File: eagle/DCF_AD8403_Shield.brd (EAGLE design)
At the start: 81 x 53.3 mm, 24 parts, among them IC1 TL072P, IC2 AD8403-100, J1 DCIN

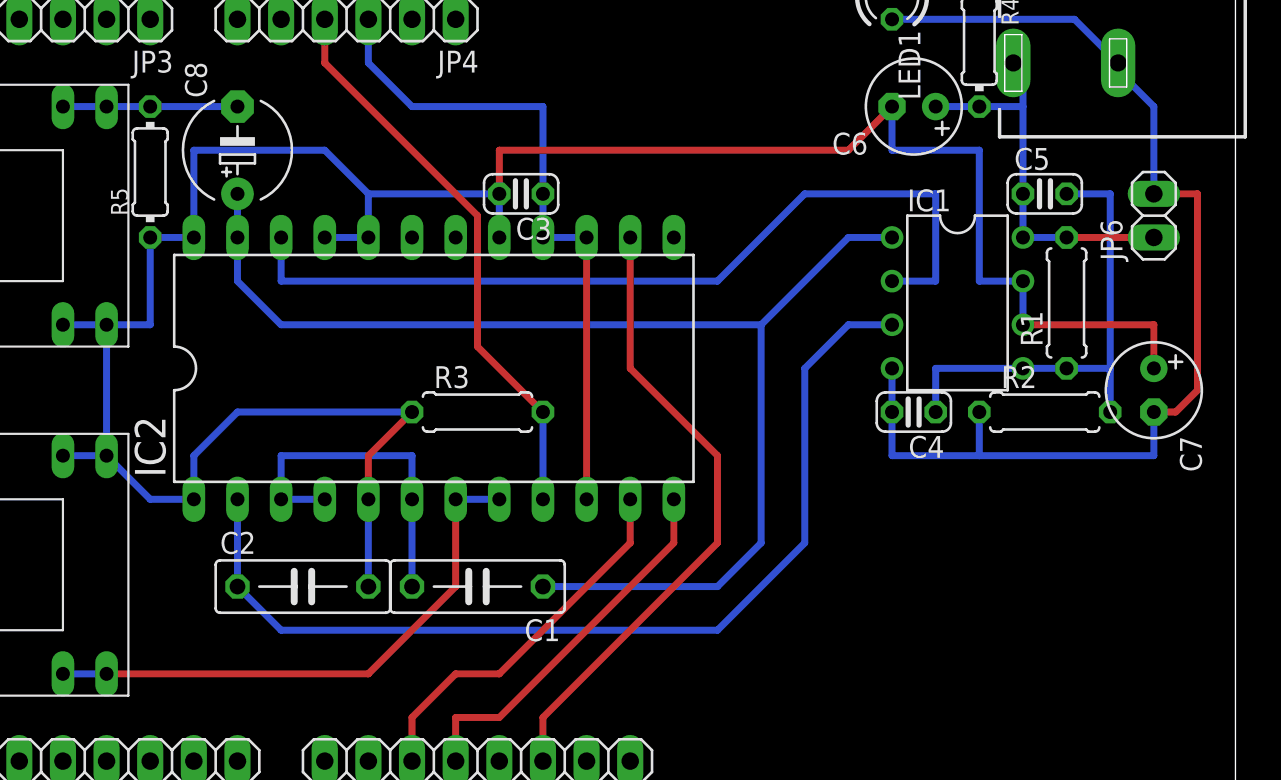
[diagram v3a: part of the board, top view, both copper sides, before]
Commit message: Remove: Decoupling Capacitor of OPAMP
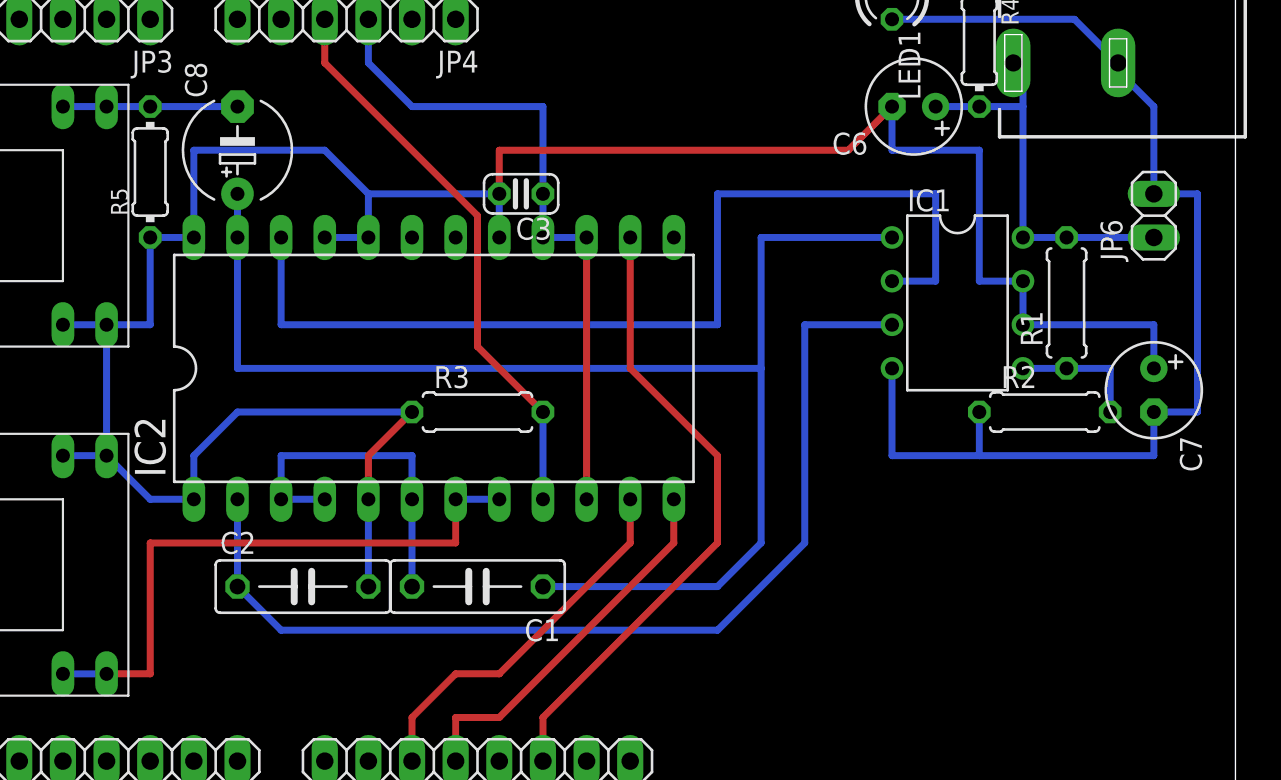
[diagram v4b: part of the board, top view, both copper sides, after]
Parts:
- removed C4, C5: 0.1uF, rcl:C025-024X044
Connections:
- net N$5: no longer C4.1, C5.2
- net V+: no longer C5.1
- net V-: no longer C4.2
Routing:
- net N$5: track 27.9 -> 7.62 mm
- net N$1: track 50.4 -> 58.4 mm
- net FILTERED: track 72.8 -> 79.8 mm
- net BYPASS: track 32.6 -> 35.6 mm
- net N$8: track 57.5 -> 59.0 mm
- net V-: track 65.1 -> 65.9 mm
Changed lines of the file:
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@@
 <element name="R1" library="rcl" package="0207/7" value="100k" x="71.12" y="31.75" rot="R90"/>
 <element name="R2" library="rcl" package="0207/7" value="100k" x="69.85" y="25.4"/>
-<element name="C4" library="rcl" package="C025-024X044" value="0.1uF" x="62.23" y="25.4" rot="R180"/>
-<element name="C5" library="rcl" package="C025-024X044" value="0.1uF" x="69.85" y="38.1"/>
 <element name="C6" library="rcl" package="E2,5-6" value="100uF" x="62.23" y="43.18" rot="R180"/>
 <element name="C7" library="rcl" package="E2,5-6" value="100uF" x="76.2" y="26.67" rot="R270"/>
@@
 <wire x1="12.7" y1="10.16" x2="15.24" y2="10.16" width="0.4064" layer="16"/>
 <wire x1="35.56" y1="20.32" x2="38.1" y2="20.32" width="0.4064" layer="16"/>
-<wire x1="15.24" y1="10.16" x2="30.48" y2="10.16" width="0.4064" layer="1"/>
-<wire x1="30.48" y1="10.16" x2="35.56" y2="15.24" width="0.4064" layer="1"/>
-<wire x1="35.56" y1="15.24" x2="35.56" y2="20.32" width="0.4064" layer="1"/>
+<wire x1="17.78" y1="17.78" x2="35.56" y2="17.78" width="0.4064" layer="1"/>
+<wire x1="35.56" y1="17.78" x2="35.56" y2="20.32" width="0.4064" layer="1"/>
+<wire x1="15.24" y1="10.16" x2="17.78" y2="10.16" width="0.4064" layer="1"/>
+<wire x1="17.78" y1="10.16" x2="17.78" y2="17.78" width="0.4064" layer="1"/>
 </signal>
 <signal name="+5V">
@@
 <wire x1="25.4" y1="12.7" x2="50.8" y2="12.7" width="0.4064" layer="16"/>
 <wire x1="50.8" y1="12.7" x2="55.88" y2="17.78" width="0.4064" layer="16"/>
-<wire x1="55.88" y1="17.78" x2="55.88" y2="27.94" width="0.4064" layer="16"/>
-<wire x1="58.42" y1="30.48" x2="60.96" y2="30.48" width="0.4064" layer="16"/>
-<wire x1="55.88" y1="27.94" x2="58.42" y2="30.48" width="0.4064" layer="16"/>
+<wire x1="55.88" y1="17.78" x2="55.88" y2="30.48" width="0.4064" layer="16"/>
+<wire x1="55.88" y1="30.48" x2="60.96" y2="30.48" width="0.4064" layer="16"/>
 </signal>
 <signal name="FILTERED">
@@
 <contactref element="IC1" pad="1"/>
 <contactref element="IC2" pad="23"/>
-<wire x1="22.86" y1="35.56" x2="22.86" y2="33.02" width="0.4064" layer="16"/>
-<wire x1="22.86" y1="33.02" x2="25.4" y2="30.48" width="0.4064" layer="16"/>
-<wire x1="25.4" y1="30.48" x2="53.34" y2="30.48" width="0.4064" layer="16"/>
+<wire x1="22.86" y1="35.56" x2="22.86" y2="27.94" width="0.4064" layer="16"/>
+<wire x1="22.86" y1="27.94" x2="53.34" y2="27.94" width="0.4064" layer="16"/>
 <wire x1="40.64" y1="15.24" x2="50.8" y2="15.24" width="0.4064" layer="16"/>
 <wire x1="50.8" y1="15.24" x2="53.34" y2="17.78" width="0.4064" layer="16"/>
-<wire x1="53.34" y1="17.78" x2="53.34" y2="30.48" width="0.4064" layer="16"/>
-<wire x1="53.34" y1="30.48" x2="58.42" y2="35.56" width="0.4064" layer="16"/>
-<wire x1="58.42" y1="35.56" x2="60.96" y2="35.56" width="0.4064" layer="16"/>
+<wire x1="53.34" y1="17.78" x2="53.34" y2="27.94" width="0.4064" layer="16"/>
+<wire x1="53.34" y1="27.94" x2="53.34" y2="35.56" width="0.4064" layer="16"/>
+<wire x1="53.34" y1="35.56" x2="60.96" y2="35.56" width="0.4064" layer="16"/>
 <contactref element="C8" pad="+"/>
 <wire x1="22.86" y1="38.1" x2="22.86" y2="35.56" width="0.4064" layer="16"/>
@@
 <contactref element="IC1" pad="2"/>
 <contactref element="IC2" pad="22"/>
-<wire x1="25.4" y1="35.56" x2="25.4" y2="33.02" width="0.4064" layer="16"/>
+<wire x1="25.4" y1="35.56" x2="25.4" y2="30.48" width="0.4064" layer="16"/>
 <wire x1="63.5" y1="33.02" x2="60.96" y2="33.02" width="0.4064" layer="16"/>
-<wire x1="25.4" y1="33.02" x2="50.8" y2="33.02" width="0.4064" layer="16"/>
-<wire x1="55.88" y1="38.1" x2="63.5" y2="38.1" width="0.4064" layer="16"/>
+<wire x1="25.4" y1="30.48" x2="50.8" y2="30.48" width="0.4064" layer="16"/>
+<wire x1="50.8" y1="38.1" x2="63.5" y2="38.1" width="0.4064" layer="16"/>
 <wire x1="63.5" y1="38.1" x2="63.5" y2="33.02" width="0.4064" layer="16"/>
-<wire x1="50.8" y1="33.02" x2="55.88" y2="38.1" width="0.4064" layer="16"/>
+<wire x1="50.8" y1="30.48" x2="50.8" y2="38.1" width="0.4064" layer="16"/>
 </signal>
 <signal name="N$5">
@@
 <contactref element="R1" pad="1"/>
 <contactref element="IC1" pad="5"/>
-<contactref element="C5" pad="2"/>
-<contactref element="C4" pad="1"/>
-<wire x1="71.12" y1="38.1" x2="73.66" y2="38.1" width="0.4064" layer="16"/>
-<wire x1="73.66" y1="38.1" x2="73.66" y2="27.94" width="0.4064" layer="16"/>
 <wire x1="73.66" y1="27.94" x2="73.66" y2="25.4" width="0.4064" layer="16"/>
 <wire x1="71.12" y1="27.94" x2="73.66" y2="27.94" width="0.4064" layer="16"/>
 <wire x1="71.12" y1="27.94" x2="68.58" y2="27.94" width="0.4064" layer="16"/>
-<wire x1="63.5" y1="25.4" x2="63.5" y2="27.94" width="0.4064" layer="16"/>
-<wire x1="63.5" y1="27.94" x2="68.58" y2="27.94" width="0.4064" layer="16"/>
 </signal>
 <signal name="SCK">
@@
 <contactref element="C6" pad="+"/>
 <contactref element="J1" pad="1"/>
-<contactref element="C5" pad="1"/>
 <contactref element="IC1" pad="8"/>
 <contactref element="R4" pad="2"/>
 <contactref element="R1" pad="2"/>
 <wire x1="63.5" y1="43.18" x2="66.04" y2="43.18" width="0.4064" layer="16"/>
-<wire x1="68.58" y1="38.1" x2="68.58" y2="43.18" width="0.4064" layer="16"/>
 <wire x1="68.58" y1="43.18" x2="68.58" y2="45.16" width="0.4064" layer="16"/>
 <wire x1="68.58" y1="45.16" x2="68.02" y2="45.72" width="0.4064" layer="16"/>
 <wire x1="66.04" y1="43.18" x2="68.58" y2="43.18" width="0.4064" layer="16"/>
-<wire x1="68.58" y1="38.1" x2="68.58" y2="35.56" width="0.4064" layer="16"/>
 <wire x1="68.58" y1="35.56" x2="71.12" y2="35.56" width="0.4064" layer="16"/>
-<wire x1="71.12" y1="35.56" x2="76.2" y2="35.56" width="0.4064" layer="1"/>
+<wire x1="68.58" y1="35.56" x2="68.58" y2="43.18" width="0.4064" layer="16"/>
+<wire x1="71.12" y1="35.56" x2="76.2" y2="35.56" width="0.4064" layer="16"/>
 </signal>
 <signal name="V-">
@@
 <contactref element="IC1" pad="4"/>
 <contactref element="JP6" pad="2"/>
-<contactref element="C4" pad="2"/>
 <contactref element="C7" pad="-"/>
 <wire x1="60.96" y1="48.26" x2="71.58" y2="48.26" width="0.4064" layer="16"/>
@@
 <wire x1="74.12" y1="45.26" x2="76.2" y2="43.18" width="0.4064" layer="16"/>
 <wire x1="76.2" y1="43.18" x2="76.2" y2="38.1" width="0.4064" layer="16"/>
-<wire x1="60.96" y1="27.94" x2="60.96" y2="25.4" width="0.4064" layer="16"/>
-<wire x1="60.96" y1="25.4" x2="60.96" y2="22.86" width="0.4064" layer="16"/>
 <wire x1="60.96" y1="22.86" x2="66.04" y2="22.86" width="0.4064" layer="16"/>
 <wire x1="66.04" y1="22.86" x2="66.04" y2="25.4" width="0.4064" layer="16"/>
 <wire x1="76.2" y1="25.4" x2="76.2" y2="22.86" width="0.4064" layer="16"/>
 <wire x1="76.2" y1="22.86" x2="66.04" y2="22.86" width="0.4064" layer="16"/>
-<wire x1="76.2" y1="25.4" x2="77.47" y2="25.4" width="0.4064" layer="1"/>
-<wire x1="77.47" y1="25.4" x2="78.74" y2="26.67" width="0.4064" layer="1"/>
-<wire x1="78.74" y1="26.67" x2="78.74" y2="38.1" width="0.4064" layer="1"/>
-<wire x1="78.74" y1="38.1" x2="76.2" y2="38.1" width="0.4064" layer="1"/>
+<wire x1="60.96" y1="27.94" x2="60.96" y2="22.86" width="0.4064" layer="16"/>
+<wire x1="76.2" y1="25.4" x2="78.74" y2="25.4" width="0.4064" layer="16"/>
+<wire x1="78.74" y1="25.4" x2="78.74" y2="38.1" width="0.4064" layer="16"/>
+<wire x1="78.74" y1="38.1" x2="76.2" y2="38.1" width="0.4064" layer="16"/>
 </signal>
 <signal name="AGND">
@@
 <wire x1="66.04" y1="40.64" x2="60.96" y2="40.64" width="0.4064" layer="16"/>
 <wire x1="60.96" y1="40.64" x2="60.96" y2="43.18" width="0.4064" layer="16"/>
-<wire x1="68.58" y1="30.48" x2="76.2" y2="30.48" width="0.4064" layer="1"/>
-<wire x1="76.2" y1="30.48" x2="76.2" y2="27.94" width="0.4064" layer="1"/>
 <wire x1="30.48" y1="20.32" x2="30.48" y2="22.86" width="0.4064" layer="1"/>
 <wire x1="30.48" y1="22.86" x2="33.02" y2="25.4" width="0.4064" layer="1"/>
@@
 <wire x1="17.78" y1="35.56" x2="17.78" y2="30.48" width="0.4064" layer="16"/>
 <wire x1="17.78" y1="30.48" x2="15.24" y2="30.48" width="0.4064" layer="16"/>
+<wire x1="68.58" y1="30.48" x2="76.2" y2="30.48" width="0.4064" layer="16"/>
+<wire x1="76.2" y1="30.48" x2="76.2" y2="27.94" width="0.4064" layer="16"/>
 </signal>
 <signal name="N$3">

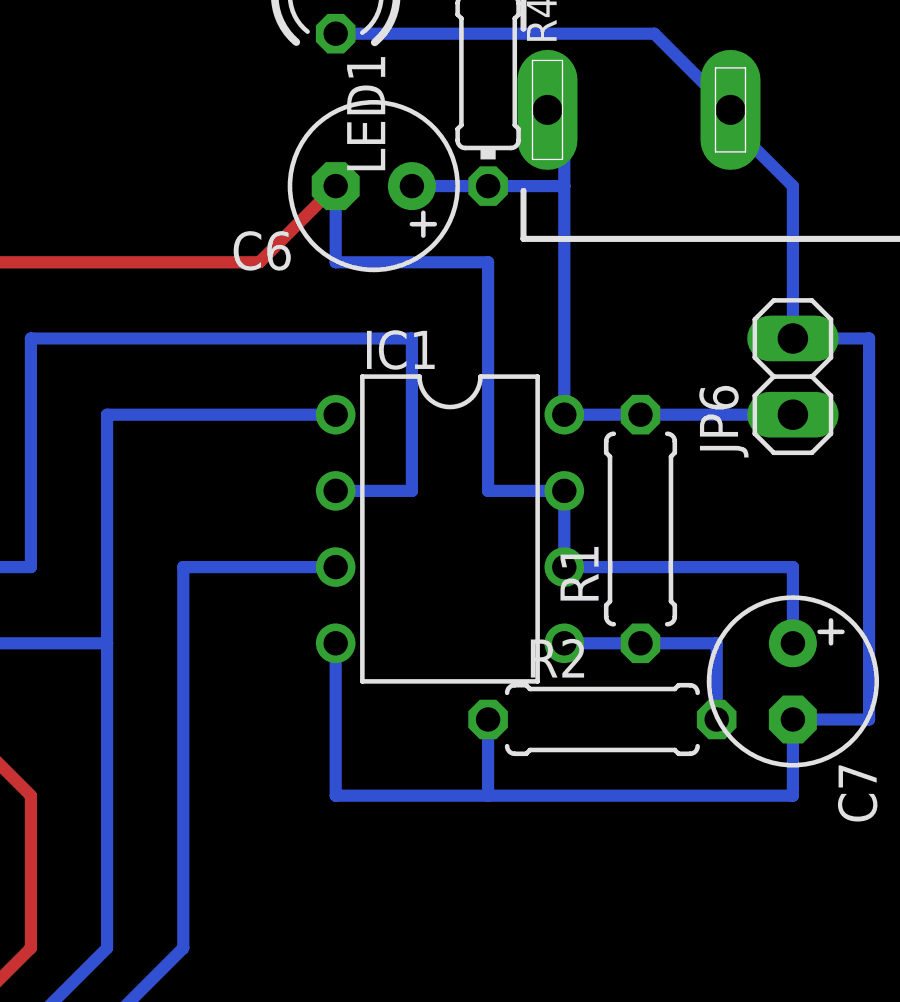
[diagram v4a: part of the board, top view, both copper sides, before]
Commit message: Add: OPAMP Decoupling Capacitor
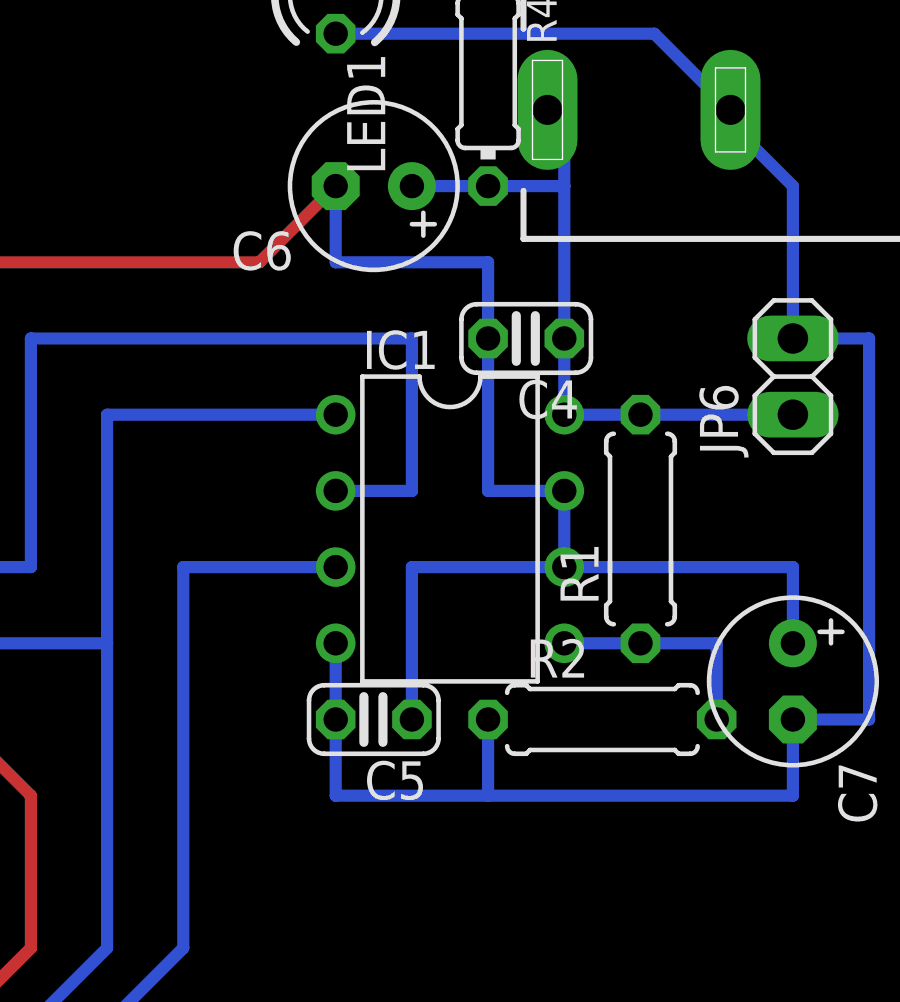
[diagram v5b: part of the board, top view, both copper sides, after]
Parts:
- added C4, C5: 0.1uF, rcl:C025-024X044
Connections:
- net AGND: now also C4.2, C5.1
- net V+: now also C4.1
- net V-: now also C5.2
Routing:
- net AGND: track 145.0 -> 155.1 mm
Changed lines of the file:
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@@
 <element name="C8" library="rcl" package="E5-6" value="10uF" x="22.86" y="40.64" rot="R90"/>
 <element name="R5" library="rcl" package="0204/7" value="10k" x="17.78" y="39.37" rot="R90"/>
+<element name="C4" library="rcl" package="C025-024X044" value="0.1uF" x="67.31" y="38.1" rot="R180"/>
+<element name="C5" library="rcl" package="C025-024X044" value="0.1uF" x="62.23" y="25.4" rot="R180"/>
 </elements>
 <signals>
@@
 <wire x1="66.04" y1="43.18" x2="68.58" y2="43.18" width="0.4064" layer="16"/>
 <wire x1="68.58" y1="35.56" x2="71.12" y2="35.56" width="0.4064" layer="16"/>
-<wire x1="68.58" y1="35.56" x2="68.58" y2="43.18" width="0.4064" layer="16"/>
 <wire x1="71.12" y1="35.56" x2="76.2" y2="35.56" width="0.4064" layer="16"/>
+<contactref element="C4" pad="1"/>
+<wire x1="68.58" y1="38.1" x2="68.58" y2="35.56" width="0.4064" layer="16"/>
+<wire x1="68.58" y1="38.1" x2="68.58" y2="43.18" width="0.4064" layer="16"/>
 </signal>
 <signal name="V-">
@@
 <wire x1="76.2" y1="25.4" x2="76.2" y2="22.86" width="0.4064" layer="16"/>
 <wire x1="76.2" y1="22.86" x2="66.04" y2="22.86" width="0.4064" layer="16"/>
-<wire x1="60.96" y1="27.94" x2="60.96" y2="22.86" width="0.4064" layer="16"/>
 <wire x1="76.2" y1="25.4" x2="78.74" y2="25.4" width="0.4064" layer="16"/>
 <wire x1="78.74" y1="25.4" x2="78.74" y2="38.1" width="0.4064" layer="16"/>
 <wire x1="78.74" y1="38.1" x2="76.2" y2="38.1" width="0.4064" layer="16"/>
+<contactref element="C5" pad="2"/>
+<wire x1="60.96" y1="27.94" x2="60.96" y2="25.4" width="0.4064" layer="16"/>
+<wire x1="60.96" y1="25.4" x2="60.96" y2="22.86" width="0.4064" layer="16"/>
 </signal>
 <signal name="AGND">
@@
 <wire x1="68.58" y1="33.02" x2="68.58" y2="30.48" width="0.4064" layer="16"/>
 <wire x1="68.58" y1="33.02" x2="66.04" y2="33.02" width="0.4064" layer="16"/>
-<wire x1="66.04" y1="33.02" x2="66.04" y2="40.64" width="0.4064" layer="16"/>
 <wire x1="66.04" y1="40.64" x2="60.96" y2="40.64" width="0.4064" layer="16"/>
 <wire x1="60.96" y1="40.64" x2="60.96" y2="43.18" width="0.4064" layer="16"/>
@@
 <wire x1="68.58" y1="30.48" x2="76.2" y2="30.48" width="0.4064" layer="16"/>
 <wire x1="76.2" y1="30.48" x2="76.2" y2="27.94" width="0.4064" layer="16"/>
+<contactref element="C5" pad="1"/>
+<contactref element="C4" pad="2"/>
+<wire x1="66.04" y1="38.1" x2="66.04" y2="40.64" width="0.4064" layer="16"/>
+<wire x1="66.04" y1="38.1" x2="66.04" y2="33.02" width="0.4064" layer="16"/>
+<wire x1="63.5" y1="25.4" x2="63.5" y2="30.48" width="0.4064" layer="16"/>
+<wire x1="63.5" y1="30.48" x2="68.58" y2="30.48" width="0.4064" layer="16"/>
 </signal>
 <signal name="N$3">

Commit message: 配線完了
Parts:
- removed J1: DCIN, con-jack:DCJ0303
- removed JP6: DCIN, pinhead:1X02
- removed R3: 0, rcl:0207/7
- C1, C2: device rcl:C075-032X103 -> rcl:C050-030X075
- IC1: value TL072P -> NJM2732
- LED1: value (none) -> GREEN
- moved LED1 9.67 mm to (57.1, 40.6), turned to 0 degrees
- moved R4 6.48 mm to (59.7, 45.7), turned to 0 degrees
- moved C2 6.35 mm to (20.3, 15.2), turned to 180 degrees
- moved C1 6.35 mm to (30.5, 15.2), turned to 0 degrees
- moved C6 5.08 mm to (67.3, 43.2)
- moved C7 2.54 mm to (76.2, 29.2)
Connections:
- removed net AGND: C2.2, C3.2, C4.2, C5.1, C6.-, C7.+, IC1.6, IC1.7, IC2.1, IC2.17, IC2.20, IC2.21, IC2.24, IC2.5, JK1.3, JK1.4, JK2.1, JK2.2, R3.1, R5.1
- removed net V+: C4.1, C6.+, IC1.8, J1.1, JP6.1, R1.2, R4.2
- removed net V-: C5.2, C7.-, IC1.4, J1.3, JP6.2, LED1.K, R2.1
- new net N$10: C2.2, C4.2, C5.1, C6.-, C7.+, IC1.6, IC1.7, IC2.21, JK1.3, JK1.4, JK2.1, JK2.2, R5.1
- net +5V: now also C4.1, C6.+, IC1.8, R1.2, R4.2
- net GND: now also C3.2, C5.2, C7.-, IC1.4, IC2.1, IC2.17, IC2.20, IC2.24, IC2.5, JP4.5, LED1.K, R2.1; no longer R3.2
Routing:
- net AGND: track 155.1 -> 0.00 mm
- net N$10: track 0.00 -> 126.4 mm
- net GND: track 33.2 -> 155.6 mm
- net V-: track 65.9 -> 0.00 mm
- net +5V: track 39.2 -> 87.4 mm
- net V+: track 23.1 -> 0.00 mm
- net FILTERED: track 79.8 -> 100.3 mm
- net N$1: track 58.4 -> 38.1 mm
- net N$8: track 59.0 -> 66.0 mm
- net SCK: track 36.8 -> 41.3 mm
- net N$6: track 20.3 -> 17.8 mm
- net MOSI: track 22.0 -> 23.5 mm
- net BYPASS: track 35.6 -> 34.1 mm
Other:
- board size 81 x 53.3 mm -> 78.4 x 53.3 mm
